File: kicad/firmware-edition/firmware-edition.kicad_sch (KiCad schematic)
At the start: 97 parts, among them J1 Solar Panel, J2 BATT, J3 3V3 Sensor Bus, J4 USB_C_Receptacle_USB2.0_16P, J5 I2C_3V3, J6 SWD, J7 Conn_01x01_Socket, J9 I2C_5V, Q1 BSS84, Q2 BSS84, Q3 BSS84, SW1 BOOT_DFU, SW2 RST, U1 ADP5091, U2 TPS61023DRLR, U3 MAX-M10M-00B, U4 Si4463, U5 STM32U073KCU6, Y1 30MHz

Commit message: kicad 9.0 updates
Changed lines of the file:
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@@
 (kicad_sch
-	(version 20231120)
+	(version 20250114)
 	(generator "eeschema")
-	(generator_version "8.0")
+	(generator_version "9.0")
 	(paper "A3")
+	(rectangle
+		(start 12.7 12.7)
+		(end 213.36 130.81)
+		(stroke
+			(width 0.635)
+			(type default)
+		)
+		(fill
+			(type none)
+		)
+	)
+	(rectangle
+		(start 213.36 12.7)
+		(end 407.67 81.28)
+		(stroke
+			(width 0.635)
+			(type default)
+		)
+		(fill
+			(type none)
+		)
+	)
+	(rectangle
+		(start 213.36 81.28)
+		(end 407.67 157.48)
+		(stroke
+			(width 0.635)
+			(type default)
+		)
+		(fill
+			(type none)
+		)
+	)
+	(text "GPS\n"
+		(exclude_from_sim no)
+		(at 363.982 25.4 0)
+		(effects
+			(font
+				(size 5.08 5.08)
+				(bold yes)
+			)
+		)
+	)
+	(text "Power Subsystem\n"
+		(exclude_from_sim no)
+		(at 165.608 24.892 0)
+		(effects
+			(font
+				(size 5.08 5.08)
+				(bold yes)
+			)
+		)
+	)
+	(text "MCU\n"
+		(exclude_from_sim no)
+		(at 113.792 156.972 0)
+		(effects
+			(font
+				(size 5.08 5.08)
+				(bold yes)
+			)
+		)
+	)
+	(text "pulldown draws quiescent but\nnecessary to avoid potential\nMCU frying\n"
+		(exclude_from_sim no)
+		(at 120.396 107.95 0)
+		(effects
+			(font
+				(size 1.27 1.27)
+			)
+		)
+	)
+	(text "VHF RX/TX\n"
+		(exclude_from_sim no)
+		(at 326.39 95.758 0)
+		(effects
+			(font
+				(size 5.08 5.08)
+				(thickness 1.016)
+				(bold yes)
+			)
+		)
+	)
+	(text "intended float of GND pin 18, see datasheet\n"
+		(exclude_from_sim no)
+		(at 276.098 151.13 0)
+		(effects
+			(font
+				(size 1.27 1.27)
+			)
+		)
+	)
 	(junction
 		(at 322.58 118.11)
@@
 		)
 	)
-	(rectangle
-		(start 12.7 12.7)
-		(end 213.36 130.81)
-		(stroke
-			(width 0.635)
-			(type default)
-		)
-		(fill
-			(type none)
-		)
-	)
-	(rectangle
-		(start 213.36 12.7)
-		(end 407.67 81.28)
-		(stroke
-			(width 0.635)
-			(type default)
-		)
-		(fill
-			(type none)
-		)
-	)
-	(rectangle
-		(start 213.36 81.28)
-		(end 407.67 157.48)
-		(stroke
-			(width 0.635)
-			(type default)
-		)
-		(fill
-			(type none)
-		)
-	)
-	(text "GPS\n"
-		(exclude_from_sim no)
-		(at 363.982 25.4 0)
-		(effects
-			(font
-				(size 5.08 5.08)
-				(bold yes)
-			)
-		)
-	)
-	(text "Power Subsystem\n"
-		(exclude_from_sim no)
-		(at 165.608 24.892 0)
-		(effects
-			(font
-				(size 5.08 5.08)
-				(bold yes)
-			)
-		)
-	)
-	(text "MCU\n"
-		(exclude_from_sim no)
-		(at 113.792 156.972 0)
-		(effects
-			(font
-				(size 5.08 5.08)
-				(bold yes)
-			)
-		)
-	)
-	(text "pulldown draws quiescent but\nnecessary to avoid potential\nMCU frying\n"
-		(exclude_from_sim no)
-		(at 120.396 107.95 0)
-		(effects
-			(font
-				(size 1.27 1.27)
-			)
-		)
-	)
-	(text "VHF RX/TX\n"
-		(exclude_from_sim no)
-		(at 326.39 95.758 0)
-		(effects
-			(font
-				(size 5.08 5.08)
-				(thickness 1.016)
-				(bold yes)
-			)
-		)
-	)
-	(text "intended float of GND pin 18, see datasheet\n"
-		(exclude_from_sim no)
-		(at 276.098 151.13 0)
-		(effects
-			(font
-				(size 1.27 1.27)
-			)
-		)
-	)
 	(label "SCL_5V"
 		(at 289.56 199.39 180)
-		(fields_autoplaced yes)
 		(effects
 			(font
@@
 	(label "SCL_3V3"
 		(at 129.54 209.55 0)
-		(fields_autoplaced yes)
 		(effects
 			(font
@@
 	(label "SETSD"
 		(at 92.71 115.57 0)
-		(fields_autoplaced yes)
 		(effects
 			(font
@@
 	(label "SETSD"
 		(at 81.28 73.66 180)
-		(fields_autoplaced yes)
 		(effects
 			(font
@@
 	(label "SDA_5V"
 		(at 289.56 201.93 180)
-		(fields_autoplaced yes)
 		(effects
 			(font
@@
 	(label "SDA_3V3"
 		(at 129.54 212.09 0)
-		(fields_autoplaced yes)
 		(effects
 			(font
@@
 	(label "SWCLK"
 		(at 129.54 222.25 0)
-		(fields_autoplaced yes)
 		(effects
 			(font
@@
 	(label "SWDIO"
 		(at 129.54 219.71 0)
-		(fields_autoplaced yes)
 		(effects
 			(font
@@
 		)
 	)
+	(embedded_fonts no)
 )

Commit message: bring updated boards into final design
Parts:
- removed C0: 470p, symbol Device:C
- removed Lchk: 390n, symbol Device:L
- removed R14: 1.47M, symbol Device:R_Small
- removed TP1, TP10, TP2, TP3, TP6, TP9: TestPoint, symbol Connector:TestPoint
- added C24: 10p, Capacitor_SMD:C_0603_1608Metric, symbol Device:C
- added C25: 470p, Capacitor_SMD:C_0402_1005Metric, symbol Device:C
- added C7: 10u, Capacitor_SMD:C_0603_1608Metric, symbol Device:C
- added C8, C9: DNP, Capacitor_SMD:C_0603_1608Metric, symbol Device:C
- added D1: 3.3V, Diode_SMD:D_0402_1005Metric_Pad0.77x0.64mm_HandSolder, symbol Device:D_Zener
- added J10, J12, J8: GPIO, Connector_PinHeader_2.54mm:PinHeader_1x02_P2.54mm_Vertical, symbol Connector_Generic:Conn_01x02
- added J13: SPI, Connector_PinHeader_2.54mm:PinHeader_1x04_P2.54mm_Vertical, symbol Connector_Generic:Conn_01x04
- added L3: 2.0n, Inductor_SMD:L_0603_1608Metric, symbol Device:L
- added Lchk1: 390n, Inductor_SMD:L_0402_1005Metric, symbol Device:L
- added R14: 10M, Resistor_SMD:R_0603_1608Metric, symbol Device:R
- added R16: 200k, Resistor_SMD:R_0603_1608Metric, symbol Device:R_Small
- added R26: 0, Resistor_SMD:R_0603_1608Metric, symbol Device:R
- AE1: footprint (none) -> PicoAPRS-CustomFootprints:AC30157-01 GNSS Ceramic Chip
- AE2: footprint (none) -> Connector_Wire:SolderWirePad_1x01_SMD_1x2mm
- C1, C2, C3, C4, C5, C6: footprint (none) -> Capacitor_SMD:C_0603_1608Metric
- C10: value 100n -> 1u
- C12: value 100n -> 2.2u; footprint (none) -> Capacitor_SMD:C_0402_1005Metric
- C13, CC1, CF2, CF3, CR2: footprint (none) -> Capacitor_SMD:C_0402_1005Metric
- C14: value 470p -> 100n; footprint (none) -> Capacitor_SMD:C_0402_1005Metric
- C15: value 100p -> 470p; footprint (none) -> Capacitor_SMD:C_0402_1005Metric
- C16: value 2.2u -> 100p; footprint (none) -> Capacitor_SMD:C_0402_1005Metric
- CF1: value 36p -> 30p; footprint (none) -> Capacitor_SMD:C_0402_1005Metric
- CR1: value 14p -> 13p; footprint (none) -> Capacitor_SMD:C_0402_1005Metric
- J1, J2, J3: footprint (none) -> Connector_PinSocket_2.54mm:PinSocket_1x02_P2.54mm_Vertical
- JP1, JP2: footprint (none) -> Jumper:SolderJumper-3_P1.3mm_Bridged12_Pad1.0x1.5mm
- L1: footprint (none) -> Inductor_SMD:L_Vishay_IFSC-1515AH_4x4x1.8mm
- L2: footprint (none) -> Inductor_SMD:L_0603_1608Metric
- LF1: value 33n -> 39n; footprint (none) -> Inductor_SMD:L_0402_1005Metric
- LF2, LF3, LF4, LR1: footprint (none) -> Inductor_SMD:L_0402_1005Metric
- LR2: value 180n -> 150n; footprint (none) -> Inductor_SMD:L_0402_1005Metric
- R1, R2: footprint (none) -> Resistor_SMD:R_0603_1608Metric
- R10: value 4.32M -> 5.1M; footprint (none) -> Resistor_SMD:R_0603_1608Metric
- R11: value 9.76M -> 10M; footprint (none) -> Resistor_SMD:R_0603_1608Metric
- R12: value 4.99M -> 4.7M; footprint (none) -> Resistor_SMD:R_0603_1608Metric
- R13: value 10.2M -> 10M; footprint (none) -> Resistor_SMD:R_0603_1608Metric
- R15: value 200k -> 1.47M; footprint (none) -> Resistor_SMD:R_0603_1608Metric
- R25: value 10M -> 0; footprint (none) -> Resistor_SMD:R_0603_1608Metric
- R3: value 6.98M -> 7.5M; footprint (none) -> Resistor_SMD:R_0603_1608Metric
- R4: value 499k -> 115k; footprint (none) -> Resistor_SMD:R_0603_1608Metric
- R5: value 2.67M -> 3.3M; footprint (none) -> Resistor_SMD:R_0603_1608Metric
- R6: value 7.15M -> 7.5M; footprint (none) -> Resistor_SMD:R_0603_1608Metric
- R7: value 8.45M -> 7.5M; footprint (none) -> Resistor_SMD:R_0603_1608Metric
- R8: value 4.7M -> 5.1M; footprint (none) -> Resistor_SMD:R_0603_1608Metric
- R9: value 18M -> 20M; footprint (none) -> Resistor_SMD:R_0603_1608Metric
- RF1: footprint (none) -> Resistor_SMD:R_0402_1005Metric
- U4: footprint Package_DFN_QFN:QFN-20-1EP_4x4mm_P0.5mm_EP2.6x2.6mm_ThermalVias -> Package_DFN_QFN:QFN-20-1EP_4x4mm_P0.5mm_EP2.6x2.6mm
- Y1: footprint (none) -> Crystal:Crystal_SMD_Abracon_ABM3-2Pin_5.0x3.2mm
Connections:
- net +3.3V: now also Lchk1.1
- net +5V: now also R15.1
- net 5V_EN: now also R14.1; no longer R25.1
- net GND: now also U4.21 (GND), U4.5 (NC), C24.2, C7.2, C8.1, C9.1, D1.2 (A), R14.2, R16.2, R26.1; no longer R15.2
- net MISO: now also J13.3 (Pin_3)
- net MOSI: now also J13.2 (Pin_2)
- net SCLK: now also J13.4 (Pin_4)
- net ~{RF_CS}: now also J13.1 (Pin_1)
- net ~{RF_EN}: now also J12.2 (Pin_2)
- net ~{RF_IRQ}: now also J12.1 (Pin_1)
- net at J2.1 (Pin_1), U1.17 (BAT): now also C7.1
- net at CF1.1, CR2.2, LF1.2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: now also C25.2
- net at U4.4 (TX): now also C25.1, Lchk1.2
- net at C2.1, J1.2 (Pin_2), L1.1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: now also D1.1 (K)
- net at U2.1 (FB): now also R15.2, R16.1; no longer R15.1
- net at AE1.1 (A): now also C24.1, R26.2; no longer U3.11 (RF_IN)
- net GPIO1: now reaches U4.10 (GPIO1)
- net GPIO1: now also J8.1 (Pin_1)
- net at U4.18 (GND): no longer U4.21 (GND)
- net GPIO2: now reaches U4.19 (GPIO2)
- net GPIO2: now also J10.2 (Pin_2)
- net GPIO3: now reaches U4.20 (GPIO3)
- net GPIO3: now also J10.1 (Pin_1)
- net GPIO0: now reaches U4.9 (GPIO0)
- net GPIO0: now also J8.2 (Pin_2)
- new net: C9.2, L3.1, R25.1
- new net: C8.2, L3.2, U3.11 (RF_IN)
- no-connect marks 22 -> 18

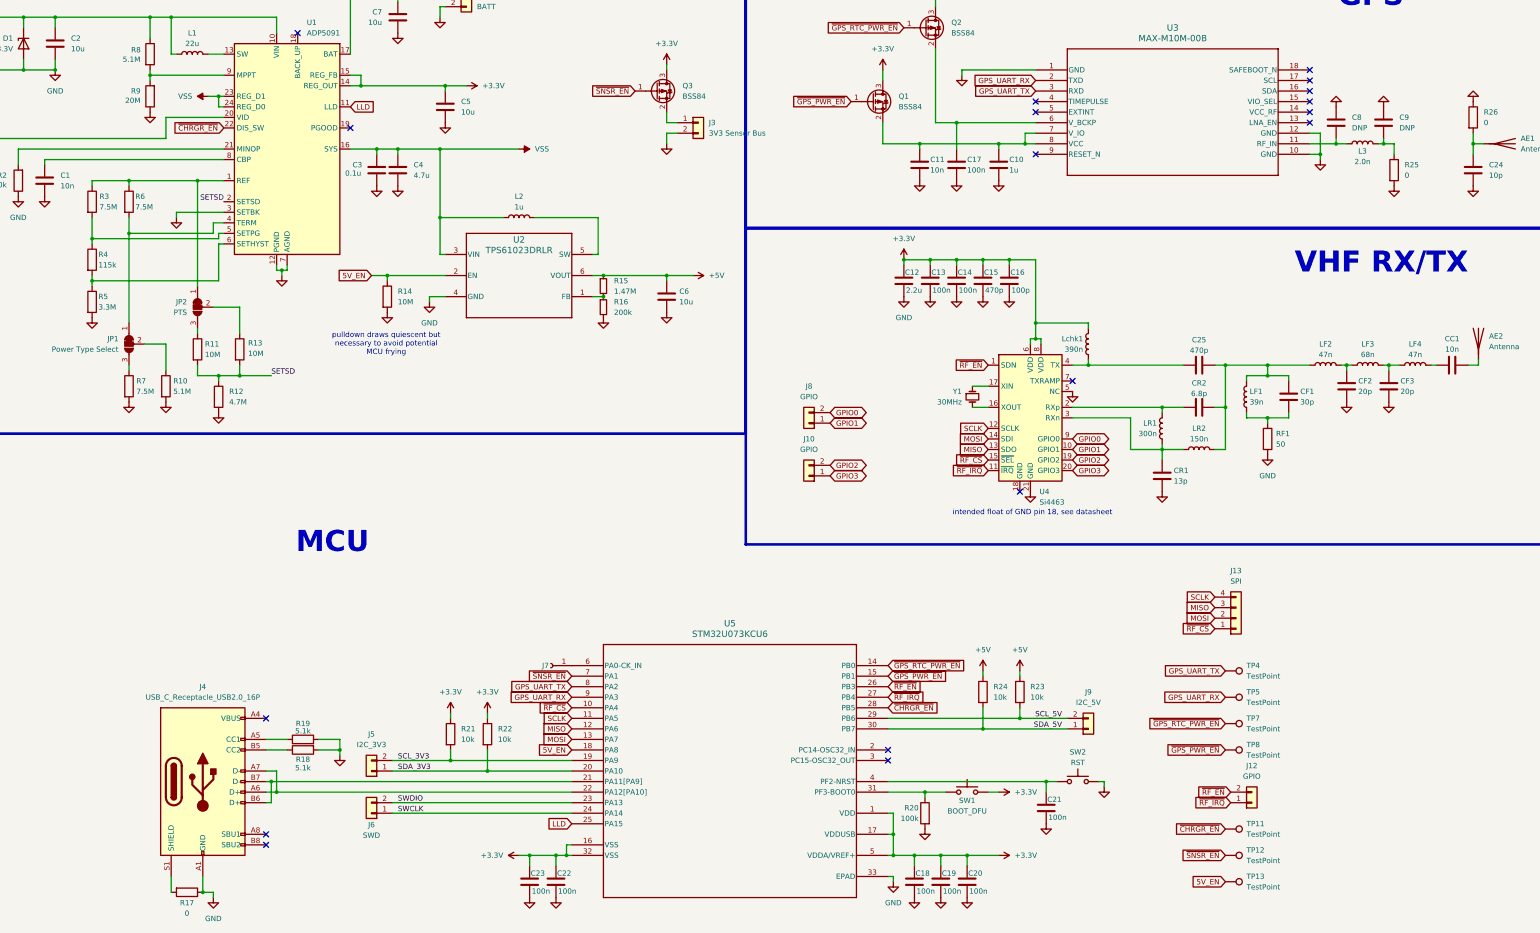
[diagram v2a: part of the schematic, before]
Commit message: update GPS to I2C
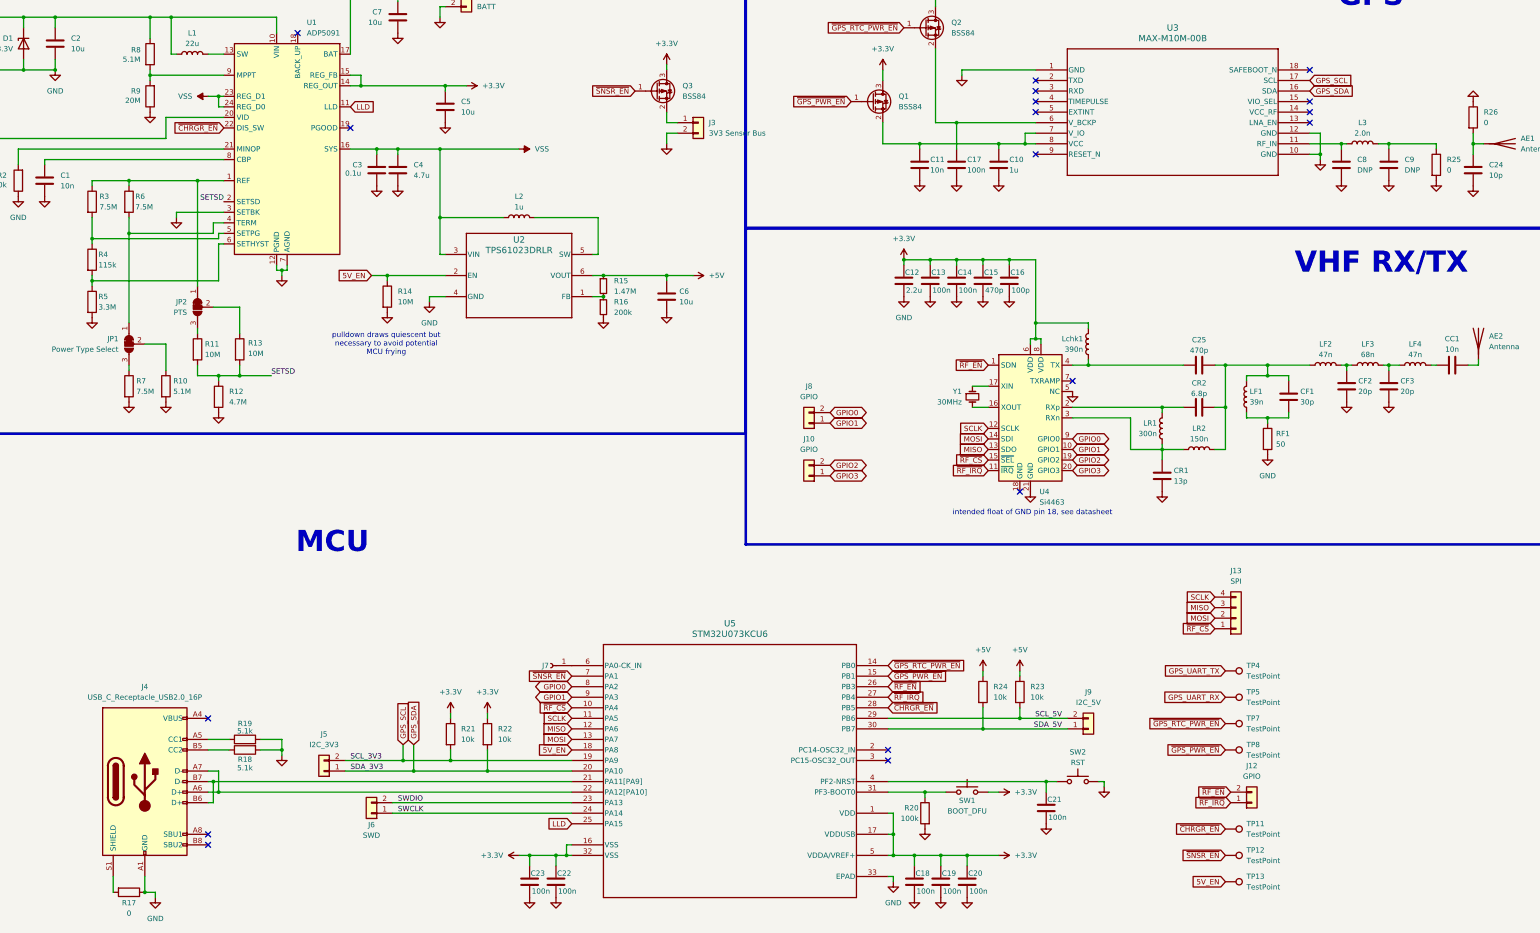
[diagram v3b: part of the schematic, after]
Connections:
- net SCL_3V3 is gone; now on net GPS_SCL: J5.2 (Pin_2), R21.2, U5.19 (PA9)
- net SDA_3V3 is gone; now on net GPS_SDA: J5.1 (Pin_1), R22.2, U5.20 (PA10)
- net GND: now also C8.2, C9.2; no longer C8.1, C9.1
- net GPIO0: now also U5.8 (PA2)
- net GPIO1: now also U5.9 (PA3)
- net GPS_UART_RX: no longer U3.2 (TXD), U5.9 (PA3)
- net GPS_UART_TX: no longer U3.3 (RXD), U5.8 (PA2)
- net at L3.1, R25.1: now also C9.1; no longer C9.2
- net at L3.2, U3.11 (RF_IN): now also C8.1; no longer C8.2
- net GPS_SDA: now reaches U3.16 (SDA)
- net GPS_SCL: now reaches U3.17 (SCL)
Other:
- moved on the sheet: C8, C9, J4, J5, R17, R18, R19, R25
